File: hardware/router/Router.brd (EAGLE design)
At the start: 133.3 x 100 mm, 38 parts, among them J1 AVR_PROG, J10 RJ45-8PTH, J11 RJ45-8PTH, J12 RJ45-8PTH, J13 RJ45-8PTH, J14 RJ45-8PTH, J15 RJ45-8PTH, J16 RJ45-8PTH, J17 RASPBERRYPI_BB, J2 RJ45-8PTH, J3 RJ45-8PTH, J4 RJ45-8PTH, J5 RJ45-8PTH, J6 RJ45-8PTH, J7 RJ45-8PTH, J8 RJ45-8PTH, J9 RJ45-8PTH, Q1 NMOS, Q2 NMOS, Q3 NMOS, U1 ATMEGA168, U2 VREG-5V-LDO-AP1117SOT89-3L, U3 DS1302_SMT, X1 1X2-C

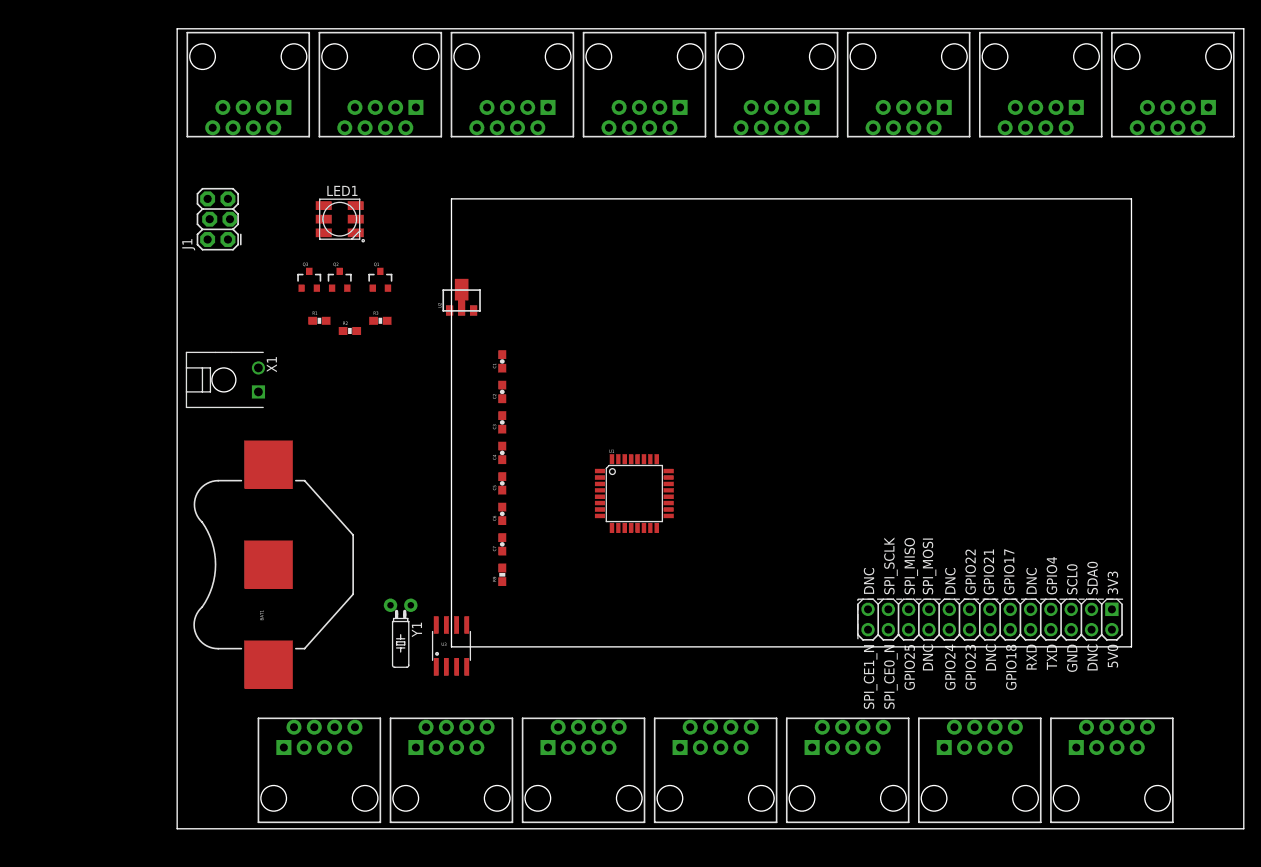
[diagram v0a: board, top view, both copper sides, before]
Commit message: Added Dispenser Schematic and Layout
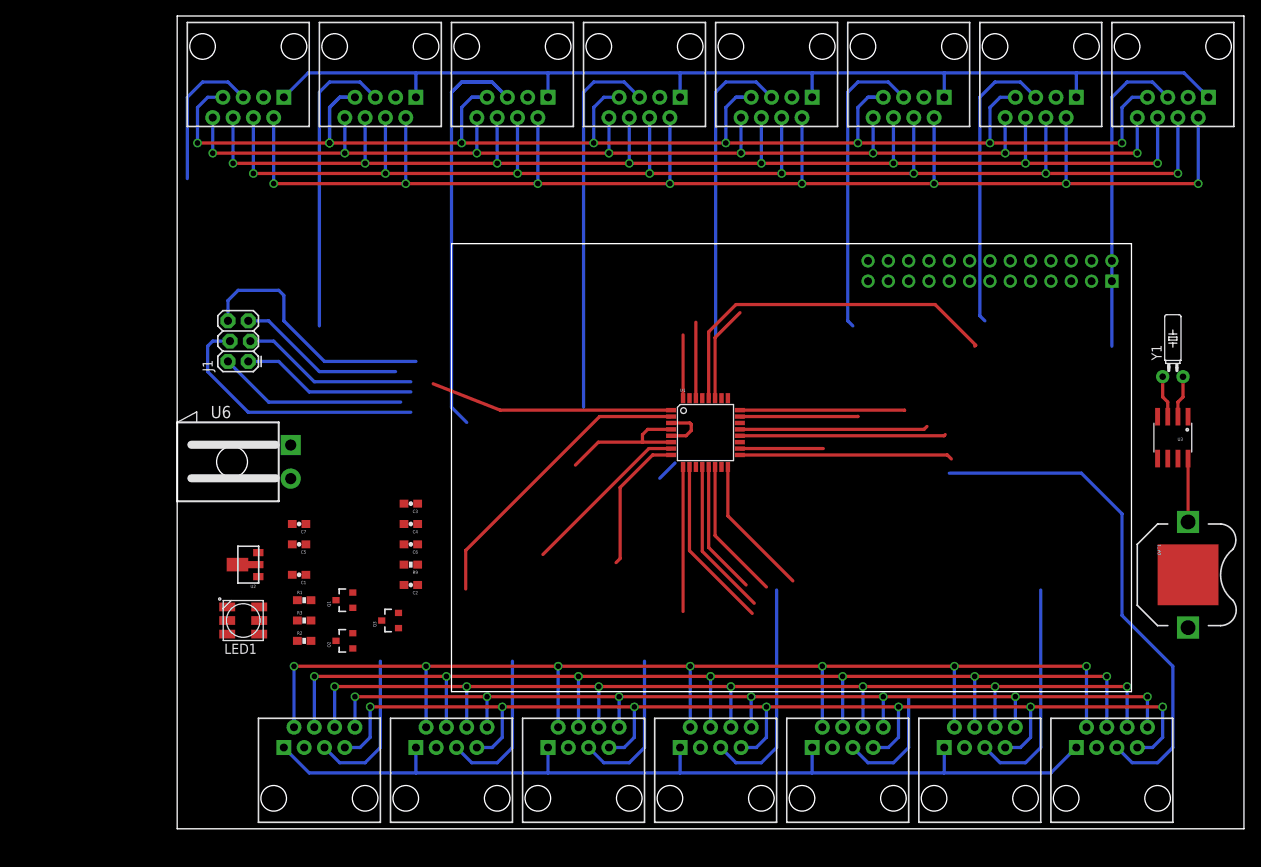
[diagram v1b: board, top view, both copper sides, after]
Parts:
- removed X1: 1X2-C, con-amp-micro-mate-n-lock:2-1445055-2
- added U6: CON-MATENLOK, pierre:MINIMATENLOK-2RA
- BAT1: value (none) -> 3V; device SparkFun-Electromechanical:BATTCON_20MM -> SparkFun-Electromechanical:BATTCON_12MM_PTH
- moved BAT1 114.9 mm to (126.4, 31.8), turned to 270 degrees
- moved Y1 100.7 mm to (124.5, 56.5), turned to 0 degrees
- moved U3 93.9 mm to (124.5, 48.9), turned to 180 degrees
- moved J17 61.6 mm to (34.3, 17.1), flipped to the bottom, turned to 90 degrees
- moved LED1 51.6 mm to (8.26, 26.0), turned to 180 degrees
- moved Q2 45.1 mm to (21.0, 23.5), turned to 90 degrees
- moved Q3 43.7 mm to (26.7, 26.0), turned to 90 degrees
- moved U2 42.4 mm to (8.89, 33.0), turned to 90 degrees
- moved Q1 40.3 mm to (21.0, 28.6), turned to 90 degrees
- moved R2 39.2 mm to (15.9, 23.5)
- moved R3 38.7 mm to (15.9, 26.0)
- moved C1 36.8 mm to (15.2, 31.8), turned to 180 degrees
- moved R1 35.0 mm to (15.9, 28.6)
- moved C2 26.7 mm to (29.2, 30.5), turned to 180 degrees
- moved C5 26.5 mm to (15.2, 35.6), turned to 180 degrees
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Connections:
- removed net MOT_A: C1.1, J10.1, J11.1, J12.1, J13.1, J14.1, J15.1, J16.1, J2.1, J3.1, J4.1, J5.1, J6.1, J7.1, J8.1, J9.1, U2.3
- removed net N$1: BAT1.1, U3.8
- removed net N$16: U1.5
- removed net N$17: U1.21
- removed net N$2: J17.8
- removed net N$3: J17.10
- removed net N$8: U1.18, U1.4
- removed net RX7: J5.5
- removed net RX8: J13.5
- removed net RX9: J6.5
- new net 3.3V: C3.1, C5.1, C7.1, J1.2, J17.1, R9.2, U1.18, U1.4, U1.6, U3.1
- new net BAT1+: BAT1.VCC@1, U3.8
- net 5V: now also J10.2, J11.2, J12.2, J13.2, J14.2, J15.2, J16.2, J2.2, J3.2, J4.2, J5.2, J6.2, J7.2, J8.2, J9.2; no longer C3.1, C5.1, C7.1, J1.2, J10.3, J11.3, J12.3, J13.3, J14.3, J15.3, J16.3, J17.1, J2.3, J3.3, J4.3, J5.3, J6.3, J7.3, J8.3, J9.3, R9.2, U1.6, U3.1
- net GND: now also BAT1.GND, U1.21, U1.5, U6.2; no longer BAT1.2, X1.2
- net RPI_CE: now also J17.15; no longer J17.11
- net RPI_RX: now also J17.10
- net RPI_SCLK: now also J17.11; no longer J17.15
- net RPI_TX: now also J17.8
- net RX7/MOSI: now also J5.5
- net RX8/MISO: now also J13.5
- net RX9/SCK: now also J6.5
- net SYNC: now also J10.7, J11.7, J12.7, J13.7, J14.7, J15.7, J16.7, J2.7, J3.7, J4.7, J5.7, J6.7, J7.7, J8.7
- net VIN: now also C1.1, J10.1, J11.1, J12.1, J13.1, J14.1, J15.1, J16.1, J2.1, J3.1, J4.1, J5.1, J6.1, J7.1, J8.1, J9.1, U2.3, U6.1; no longer X1.1
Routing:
- net GND: track 0.00 -> 338.6 mm, vias 0 -> 15
- net 5V: track 0.00 -> 334.0 mm, vias 0 -> 15
- net TX: track 0.00 -> 324.5 mm, vias 0 -> 15
- net SYNC: track 0.00 -> 315.9 mm, vias 0 -> 15
- net DISP_!RST: track 0.00 -> 303.8 mm, vias 0 -> 15
- net VIN: track 0.00 -> 253.9 mm
- net RX2: track 0.00 -> 101.5 mm
- net RX9/SCK: track 0.00 -> 87.6 mm
- net RX0: track 0.00 -> 87.3 mm
- net RX8/MISO: track 0.00 -> 67.8 mm
- net RX11: track 0.00 -> 58.1 mm
- net RX13: track 0.00 -> 57.4 mm
- net RX3: track 0.00 -> 55.6 mm
- net 3.3V: track 0.00 -> 52.1 mm
- net RX5: track 0.00 -> 50.4 mm
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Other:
- board size 133.3 x 100 mm -> 133.3 x 101.6 mm

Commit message: Updated Router Schematic with DS1307 and Accessory Port
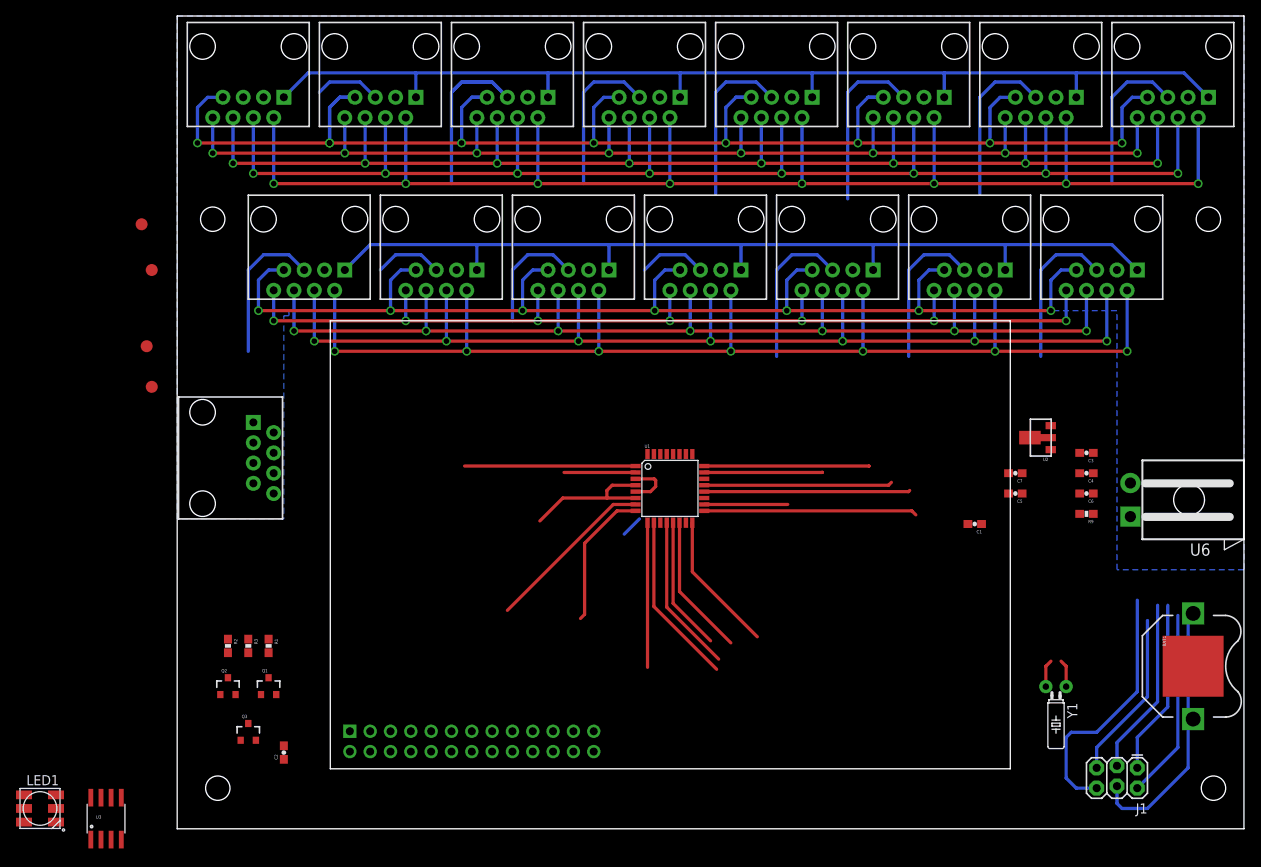
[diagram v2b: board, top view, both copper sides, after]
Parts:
- added J18: RJ45-8PTH, SparkFun:RJ45-8
- added JP1, JP2, JP3, JP4: FIDUCIAL1.5X3, SparkFun-Aesthetics:FIDUCIAL-1.5X3
- added JP5, JP6, JP7, JP8: STAND-OFFTIGHT, SparkFun-Electromechanical:STAND-OFF-TIGHT
- LED1: device adafruit:RGBLED5050 -> pierre:RGBLED5050
- U3: value DS1302_SMT -> DS1307SO8; device pierre:SO08 -> SparkFun-FreqCtrl:SO08
- Y1: value (none) -> 32.768kHz
- moved U3 141.6 mm to (-8.89, 1.27), turned to 0 degrees
- moved U6 134.1 mm to (133.3, 36.2), turned to 90 degrees
- moved J10 123.7 mm to (16.5, 76.2), turned to 180 degrees
- moved J1 122.2 mm to (120.0, 7.62), turned to 180 degrees
- moved J16 121.7 mm to (115.6, 76.2), turned to 180 degrees
- moved U2 100.3 mm to (108.0, 48.9)
- moved J11 98.8 mm to (33.0, 76.2), turned to 180 degrees
- moved J15 97.1 mm to (99.1, 76.2), turned to 180 degrees
- moved C5 89.8 mm to (104.8, 41.9)
- moved C7 89.8 mm to (104.8, 44.5)
- moved C3 84.7 mm to (113.7, 47.0)
- moved C4 84.7 mm to (113.7, 44.5)
- moved C6 84.7 mm to (113.7, 41.9)
- moved R9 84.7 mm to (113.7, 39.4)
- moved C1 84.7 mm to (99.7, 38.1)
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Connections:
- net 3.3V: no longer U3.1
- net 5V: now also J18.2, LED1.1, LED1.2, LED1.3; no longer LED1.4, LED1.5, LED1.6
- net BAT1+: no longer U3.8
- net BLUE: now also Q3.1; no longer Q1.1
- net GND: now also J18.8
- net GREEN: now also Q1.1; no longer Q2.1
- net N$12: now also LED1.5; no longer LED1.1
- net N$13: now also LED1.6; no longer LED1.2
- net N$6: now also U3.1; no longer U3.3
- net N$7: no longer U3.2
- net N$9: now also LED1.4; no longer LED1.3
- net RED: now also Q2.1; no longer Q3.1
- net RPI_CE: no longer U3.5
- net RPI_I/O: no longer U3.6
- net RPI_SCL: now also J18.6, U3.6
- net RPI_SCLK: no longer U3.7
- net RPI_SDA: now also J18.4, U3.5
- net VIN: now also J18.1
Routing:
- net RX2: track 101.5 -> 27.7 mm
- net RX0: track 87.3 -> 39.1 mm
- net RPI_SCL: track 45.4 -> 0.00 mm
- net RX5: track 50.4 -> 19.7 mm
- net RX3: track 55.6 -> 26.4 mm
- net RX1: track 49.1 -> 21.4 mm
- net RX8/MISO: track 67.8 -> 48.1 mm
- net RX4: track 49.8 -> 30.1 mm
- net RX9/SCK: track 87.6 -> 69.8 mm
- net RX13: track 57.4 -> 41.2 mm
- net RX11: track 58.1 -> 42.0 mm
- net RPI_SDA: track 12.0 -> 0.00 mm
- net TX: track 324.5 -> 315.0 mm
- net BAT1+: track 7.92 -> 0.00 mm
- net DISP_!RST: track 303.8 -> 295.9 mm
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- added copper zone on layer 16, net VIN

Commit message: Commiting updated SCH and BRD
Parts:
- added C8: 47u, SparkFun-Capacitors:PANASONIC_D
- added C9: 100n, SparkFun:0603-CAP
- added FRAME3: FRAME-LETTER, SparkFun-Aesthetics:CREATIVE_COMMONS
- added J19: RJ45-8PTH, SparkFun:RJ45-8
- added JP9: STAND-OFFTIGHT, SparkFun-Electromechanical:STAND-OFF-TIGHT
- added U$5: OSHW-LOGOS, SparkFun-Aesthetics:OSHW-LOGO-S
- U2: value VREG-5V-LDO-AP1117SOT89-3L -> (none); device pierre:SOT89-3L -> SparkFun-PowerIC:78XXL
- moved JP2 125.9 mm to (111.1, 17.1)
- moved JP1 120.5 mm to (111.1, 41.3)
- moved U3 104.0 mm to (93.3, 20.3), turned to 180 degrees
- moved C4 88.9 mm to (24.8, 43.8), turned to 0 degrees
- moved U2 79.7 mm to (29.2, 36.8), flipped to the bottom
- moved C1 74.7 mm to (25.4, 30.5)
- moved J1 71.3 mm to (52.1, 29.2), turned to 0 degrees
- moved C2 63.1 mm to (72.4, 31.8), turned to 270 degrees
- moved JP4 52.5 mm to (41.3, 27.3)
- moved JP3 46.8 mm to (41.9, 50.2)
- moved C7 44.5 mm to (60.3, 45.1), turned to 270 degrees
- moved C3 34.4 mm to (79.4, 50.2)
- moved BAT1 33.9 mm to (95.9, 6.99), turned to 180 degrees
- moved R9 31.8 mm to (82.5, 45.7), turned to 90 degrees
- moved C6 28.6 mm to (85.1, 43.8), turned to 0 degrees
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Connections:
- removed net N$7: Y1.2
- removed net RPI_CE: J17.15
- removed net RPI_I/O: J17.13
- new net CE0: J17.24, J18.7
- new net CE1: J17.26, J19.7
- new net N$1: U3.2, Y1.1
- new net RPI_MISO: J17.21, J18.4, J19.4
- new net RPI_MOSI: J17.19, J18.5, J19.5
- net 5V: now also J19.2, U2.OUT, U3.8; no longer U2.2, U2.2.1
- net BAT1+: now also U3.3
- net BLUE: now also J17.16; no longer J17.22
- net GND: now also C8.-, C9.2, J19.8, U2.GND; no longer U2.1
- net GREEN: now also J17.22; no longer J17.18
- net N$6: now also Y1.2; no longer Y1.1
- net RED: now also J17.18; no longer J17.16
- net RPI_SCL: no longer J18.6
- net RPI_SCLK: now also J17.23, J18.6, J19.6; no longer J17.11
- net RPI_SDA: no longer J18.4
- net VIN: now also C8.+, C9.1, J19.1, U2.IN; no longer U2.3
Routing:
- net GND: track 338.6 -> 3.81 mm, vias 15 -> 0
- net 5V: track 334.0 -> 12.4 mm, vias 15 -> 0
- net RPI_SCL: track 0.00 -> 137.0 mm, vias 0 -> 2
- net RPI_SDA: track 0.00 -> 121.8 mm, vias 0 -> 2
- net CE0: track 0.00 -> 103.4 mm
- net CE1: track 0.00 -> 82.3 mm
- net RPI_SCLK: track 0.00 -> 80.4 mm, vias 0 -> 2
- net RPI_MOSI: track 0.00 -> 80.4 mm
- net RPI_MISO: track 0.00 -> 70.2 mm, vias 0 -> 1
- net RPI_TX: track 16.7 -> 69.3 mm
- net 3.3V: track 52.1 -> 0.00 mm
- net RX0: track 39.1 -> 85.8 mm
- net RX14: track 19.4 -> 64.2 mm
- net RPI_RX: track 19.7 -> 61.8 mm
- net SYNC: track 315.9 -> 357.6 mm, vias 15 -> 16
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- added copper zone on layer 1, net 5V
- added copper zone on layer 16, net GND

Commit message: Finished Router Layout!
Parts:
- J17: device microbuilder:RASBERRYPI_SHIELD -> pierre:RASBERRYPI_SHIELD
- moved J17 101.8 mm to (28.6, 7.62), flipped to the top, turned to 0 degrees
- moved C8 63.1 mm to (118.1, 5.08), turned to 0 degrees
- moved JP4 24.9 mm to (66.0, 24.8)
- moved C9 15.1 mm to (21.6, 42.5), turned to 90 degrees
- moved C7 14.9 mm to (69.8, 33.7)
- moved C5 14.8 mm to (72.4, 48.9)
- moved C1 13.4 mm to (19.7, 42.5), turned to 90 degrees
- moved C3 10.5 mm to (88.9, 45.7), turned to 90 degrees
- moved U2 7.62 mm to (29.2, 44.5)
- moved C4 4.07 mm to (21.6, 46.4), turned to 270 degrees
- moved C2 1.94 mm to (72.0, 33.7)
- moved Q1 1.27 mm to (20.3, 7.62)
- moved Q2 1.27 mm to (20.3, 12.1)
- moved Q3 1.27 mm to (20.3, 16.5)
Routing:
- net VIN: track 253.9 -> 74.7 mm
- net GND: track 3.81 -> 167.5 mm, vias 0 -> 20
- net RX1: track 6.50 -> 117.2 mm, vias 0 -> 6
- net RX13: track 27.0 -> 112.2 mm, vias 0 -> 2
- net RX2: track 24.8 -> 101.6 mm, vias 0 -> 4
- net RX11: track 33.3 -> 103.6 mm, vias 0 -> 6
- net RX9/SCK: track 47.5 -> 113.2 mm, vias 1 -> 4
- net RX3: track 26.6 -> 89.4 mm, vias 0 -> 4
- net RX7/MOSI: track 40.7 -> 100.1 mm, vias 0 -> 4
- net 5V: track 12.4 -> 70.7 mm
- net DISP_!RST: track 294.4 -> 348.6 mm, vias 13 -> 15
- net SYNC: track 357.6 -> 397.9 mm, vias 16 -> 2
- net RX4: track 36.2 -> 70.9 mm, vias 0 -> 1
- net RX8/MISO: track 35.0 -> 69.3 mm
- net RX0: track 85.8 -> 115.8 mm, vias 0 -> 4
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- added copper zone on layer 1, net 3.3V
